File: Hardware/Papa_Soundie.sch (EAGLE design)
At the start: 79 parts, among them J1 Audio Jack, J2 MICRO-SD_CARD_SOCKET, U1 ATMEGA328P_TQFP, U2 VS1000D, U3 3.3V, U4 4MB Flash, Y1 12MHz, Y2 8MHz

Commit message: updating silk, cleaning sch
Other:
- note added: "ANALOG"
- note added: "Audio Out"
- note added: "Digital IO/SPI"
- note added: "FTDI Connector"
- note added: "I2C"
- note added: "Left and Right AC coupled audio channels"
- note added: "RESET"
- note added: "TX and RX of the VLSI chip"
- note added: "USB+ and USB- of the VLSI chip"
- note added: "VIN"
- note added: "VOUT"
- note removed: "Audio Decoupling"
- moved on the sheet: C4, C5, C6, J11, J12, J3, J5, J7, J9, R11, R15

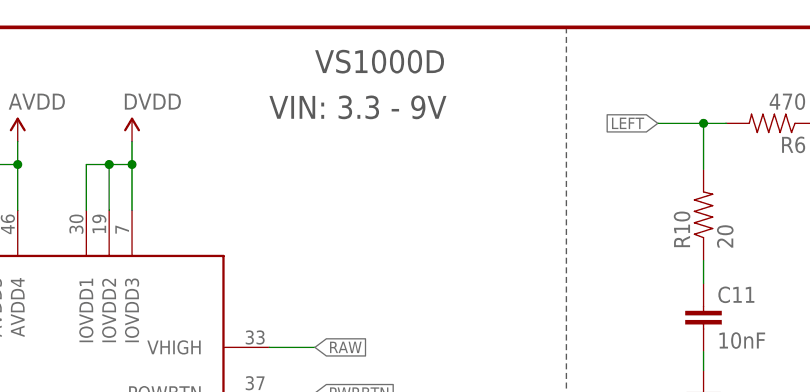
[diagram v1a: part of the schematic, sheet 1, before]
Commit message: Updated input voltage range
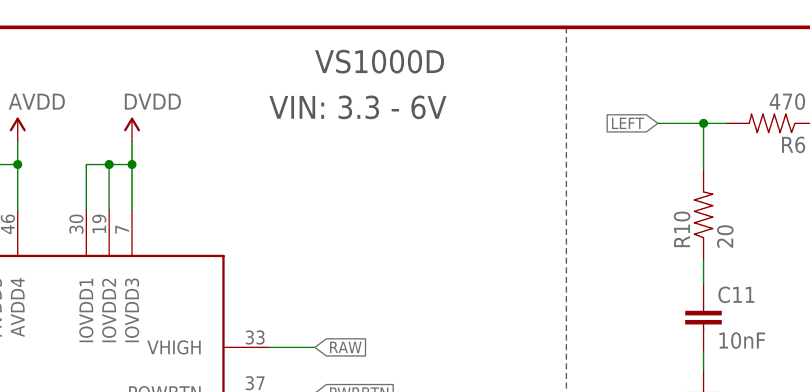
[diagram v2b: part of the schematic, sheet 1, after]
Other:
- note added: "VIN: 3.3 - 6V"
- note removed: "VIN: 3.3 - 9V"
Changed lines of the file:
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@@
 <?xml version="1.0" encoding="utf-8"?>
 <!DOCTYPE eagle SYSTEM "eagle.dtd">
-<eagle version="7.7.0">
+<eagle version="8.7.0">
 <drawing>
 <settings>
 <setting alwaysvectorfont="no"/>
+<setting keepoldvectorfont="yes"/>
 <setting verticaltext="up"/>
 </settings>
@@
 <text x="73.66" y="55.88" size="2.54" layer="97" font="vector" ratio="10">SPI Flash</text>
 <text x="114.3" y="180.34" size="2.54" layer="97" font="vector" ratio="10">VS1000D</text>
-<text x="109.22" y="175.26" size="2.54" layer="97" font="vector">VIN: 3.3 - 9V</text>
+<text x="109.22" y="175.26" size="2.54" layer="97" font="vector">VIN: 3.3 - 6V</text>
 <wire x1="210.82" y1="55.88" x2="210.82" y2="35.56" width="0.1524" layer="97" style="longdash"/>
 <wire x1="210.82" y1="55.88" x2="248.92" y2="55.88" width="0.1524" layer="97" style="longdash"/>
